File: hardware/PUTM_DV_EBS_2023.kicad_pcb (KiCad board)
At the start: 4 copper layers, 100 x 70 mm, 147 parts, among them IC1 UCC2946DG4, IC2 SN74LVC1G74DCTR, IC3 SN74LVC1G74DCTR, IC4 ACT4533AYH-T, J1 SAFETY_SUPPLY, J2 SWDIO_CONN, J3 SENSORS, J4 VALVES, J5 MAIN, K1 FINDER-30.22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

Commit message: wip
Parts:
- added REF**: TestPoint_Pad_D1.5mm, TestPoint:TestPoint_Pad_D1.5mm, F.Cu at (132.4, 107.8)
- C23: footprint Capacitor_SMD:C_0201_0603Metric_Pad0.64x0.40mm_HandSolder -> Capacitor_SMD:C_0603_1608Metric_Pad1.08x0.95mm_HandSolder
- moved G*** 113.5 mm to (120.7, 74.2), turned to 180 degrees
- moved REF** 85.6 mm to (136.5, 62.0), turned to 180 degrees
- moved C5 82.7 mm to (151.9, 42.7), turned to 90 degrees
- moved D15 63.6 mm to (157.7, 67.8)
- moved C31 63.6 mm to (154.9, 65.0)
- moved R32 63.6 mm to (158.0, 65.0)
- moved R33 63.6 mm to (156.5, 65.0)
- moved R30 58.2 mm to (141.7, 77.1), turned to -90 degrees
- moved R31 57.1 mm to (140.2, 77.1), turned to 90 degrees
- moved C30 56.0 mm to (138.7, 77.1), turned to 90 degrees
- moved R4 55.5 mm to (130.2, 73.6), turned to 0 degrees
- moved D14 55.4 mm to (140.4, 79.9), turned to 0 degrees
- moved R1 54.2 mm to (130.2, 75.4), turned to 0 degrees
- moved R14 52.8 mm to (130.2, 77.2), turned to 180 degrees
- moved R28 51.8 mm to (140.1, 82.7), turned to -90 degrees
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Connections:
- R47 pad 2: unconnected-(R47-Pad2) -> GND
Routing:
- net GND: track 74.9 -> 137.5 mm, vias 9 -> 17
- net Net-(IC1-Pad5): track 0.00 -> 37.6 mm
- net /EBS Logic/RESET BUTTON LATCH: track 0.00 -> 37.5 mm, vias 0 -> 3
- net /EBS Logic/AS COMMANDS OK: track 0.00 -> 30.4 mm, vias 0 -> 2
- net /EBS Supervisor/ERROR: track 0.00 -> 25.5 mm
- net /EBS Supervisor/CHECKUP: track 0.00 -> 24.7 mm, vias 0 -> 2
- net +3V3: track 2.21 -> 26.7 mm, vias 0 -> 2
- net VALVE_1_COIL_I: track 6.64 -> 26.3 mm
- net /EBS Logic/WATCHDOG: track 0.00 -> 18.3 mm, vias 0 -> 2
- net Net-(D12-Pad2): track 0.00 -> 17.7 mm
- net /EBS Supervisor/WARNING: track 0.00 -> 17.4 mm
- net /EBS Supervisor/OK: track 0.00 -> 15.4 mm, vias 0 -> 2
- net Net-(IC2-Pad3): track 0.00 -> 15.0 mm
- net Net-(IC3-Pad6): track 0.00 -> 14.5 mm
- net +24V: track 13.4 -> 25.4 mm
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
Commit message: fixed references addet tp;s mam pojutrze przejebany egzamin nara
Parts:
- removed the REF** at (132.4, 107.8)
- added C37: 100nF, Capacitor_SMD:C_0603_1608Metric, F.Cu at (109.7, 50.5)
- added C38: 100nF, Capacitor_SMD:C_0603_1608Metric, F.Cu at (103.6, 48.5)
- added C39: 100nF, Capacitor_SMD:C_0603_1608Metric, F.Cu at (103.4, 60.2)
- added NT1: NetTie_2, NetTie:NetTie-2_SMD_Pad0.5mm, F.Cu at (105.4, 72.9)
- added REF**: TestPoint_Pad_1.0x1.0mm, TestPoint:TestPoint_Pad_1.0x1.0mm, F.Cu at (187.2, 88.1)
- added REF**: TestPoint_Pad_1.0x1.0mm, TestPoint:TestPoint_Pad_1.0x1.0mm, F.Cu at (187.2, 81.3)
- added REF**: TestPoint_Pad_1.0x1.0mm, TestPoint:TestPoint_Pad_1.0x1.0mm, F.Cu at (187.2, 76.7)
- added REF**: TestPoint_Pad_1.0x1.0mm, TestPoint:TestPoint_Pad_1.0x1.0mm, F.Cu at (187.2, 83.6)
- added REF**: TestPoint_Pad_1.0x1.0mm, TestPoint:TestPoint_Pad_1.0x1.0mm, F.Cu at (181.9, 88.1)
- added REF**: TestPoint_Pad_1.0x1.0mm, TestPoint:TestPoint_Pad_1.0x1.0mm, F.Cu at (187.2, 85.9)
- added REF**: TestPoint_Pad_1.0x1.0mm, TestPoint:TestPoint_Pad_1.0x1.0mm, F.Cu at (181.9, 76.7)
- added REF**: TestPoint_Pad_1.0x1.0mm, TestPoint:TestPoint_Pad_1.0x1.0mm, F.Cu at (187.2, 79.0)
- added REF**: TestPoint_Pad_1.0x1.0mm, TestPoint:TestPoint_Pad_1.0x1.0mm, F.Cu at (181.9, 81.3)
- added REF**: TestPoint_Pad_1.0x1.0mm, TestPoint:TestPoint_Pad_1.0x1.0mm, F.Cu at (181.9, 83.6)
- added REF**: TestPoint_Pad_1.0x1.0mm, TestPoint:TestPoint_Pad_1.0x1.0mm, F.Cu at (181.9, 79.0)
- added REF**: TestPoint_Pad_1.0x1.0mm, TestPoint:TestPoint_Pad_1.0x1.0mm, F.Cu at (181.9, 85.9)
- C18: footprint Capacitor_SMD:C_0805_2012Metric_Pad1.18x1.45mm_HandSolder -> Capacitor_SMD:C_1206_3216Metric
- moved G*** 71.7 mm to (172.8, 94.2)
- moved D2 28.6 mm to (124.5, 37.8), turned to -135 degrees
- moved R13 20.8 mm to (125.2, 40.6), turned to 45 degrees
- moved JP1 12.4 mm to (119.4, 42.2), turned to 90 degrees
- moved R5 11.0 mm to (130.0, 73.7)
- moved R4 10.7 mm to (130.0, 84.3)
- moved C14 9.85 mm to (112.8, 59.4), turned to 180 degrees
- moved C15 9.68 mm to (106.3, 56.0)
- moved U6 9.67 mm to (110.7, 55.9)
- moved R46 6.93 mm to (96.8, 60.2), turned to 90 degrees
- moved R44 4.52 mm to (100.3, 54.6), turned to 180 degrees
- moved U10 3.65 mm to (100.1, 60.2), turned to 0 degrees
- moved C19 3.31 mm to (148.6, 57.7), turned to -90 degrees
- moved K2 3.25 mm to (165.1, 50.5)
- moved R43 3.07 mm to (97.0, 48.6)
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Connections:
- net /EBS Supervisor/CAN_RX+ renamed /EBS Supervisor/(CAN_RX)+
- net /EBS Supervisor/CAN_TX- renamed /EBS Supervisor/(CAN_TX)-
- J3 pad 1: AIR_MAIN -> AIR_EBS
- J3 pad 2: AIR_EBS -> AIR_MAIN
- R4 pad 2: /EBS Logic/WATCHDOG -> /EBS Logic/AS_CLOSE_SDC
- R5 pad 2: /EBS Logic/AS_CLOSE_SDC -> /EBS Logic/WATCHDOG
- REF** pad 1: (no net) -> GND
- U5 pad 10: /Air pressure sensor control/MAIN -> /Air pressure sensor control/REDUNDANT
- U5 pad 8: /Air pressure sensor control/REDUNDANT -> /Air pressure sensor control/MAIN
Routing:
- net /Air pressure sensor control/MAIN: track 0.00 -> 69.5 mm, vias 0 -> 2
- net /Air pressure sensor control/EBS: track 0.00 -> 50.8 mm
- net /Air pressure sensor control/REDUNDANT: track 0.00 -> 38.9 mm
- net +24V: track 25.4 -> 58.8 mm
- net /EBS Logic/RESET BUTTON LATCH: track 37.5 -> 6.04 mm, vias 3 -> 2
- net VALVE_2_COIL_I: track 6.15 -> 34.6 mm
- net Net-(IC1-Pad5): track 37.6 -> 17.8 mm
- net NRST: track 0.00 -> 16.7 mm
- net AUX1: track 0.00 -> 13.6 mm
- net CAN+: track 19.5 -> 6.48 mm
- net /EBS Logic/AS COMMANDS OK: track 30.4 -> 17.9 mm, vias 2 -> 0
- net Net-(U5-Pad21): track 0.00 -> 12.2 mm
- net CAN-: track 17.3 -> 5.92 mm, vias 2 -> 0
- net SWDCLK: track 0.00 -> 11.2 mm
- net AUX2: track 0.00 -> 11.0 mm
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- added copper zone on F.Cu, net +24V
- added copper zone on B.Cu, net +5V
- added copper zone on F.Cu, net +5V
- added copper zone on F.Cu, net /Power Supply/SW_loop
- added copper zone on F.Cu, net GND
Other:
- board text added: "AND2"
- board text added: "NAND1"
- board text added: "RST_EBS"
- board text added: "RST_LATCH"
- board text added: "RTH"
- board text added: "SDC_IN"
- board text added: "SDC_K"
- board text added: "SDC_RDY"
- board text added: "TSON_DRV"
- board text added: "TSON_EXT"
- board text added: "WDI"
- board text added: "WDO"

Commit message: supply section redesign due to IC shortage
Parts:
- removed C17: 47uF, Capacitor_SMD:CP_Elec_6.3x7.7
- removed C18: 10uF low ESR, Capacitor_SMD:C_1206_3216Metric
- removed C21: 2.2nF, Capacitor_SMD:C_0603_1608Metric_Pad1.08x0.95mm_HandSolder
- removed C22: 22nF, Capacitor_SMD:C_1206_3216Metric
- removed C24: 1nF, Capacitor_SMD:C_0603_1608Metric_Pad1.08x0.95mm_HandSolder
- removed C25: 10uF, Capacitor_SMD:C_0603_1608Metric_Pad1.08x0.95mm_HandSolder
- removed C26: 220uF, Capacitor_SMD:CP_Elec_6.3x7.7
- removed IC4: ACT4533AYH-T, SamacSys_Parts:SOIC127P600X170-9N
- removed L2: 47uH, PUTM_Kicad_FOOTPRINTS:L_Bourns_SRP1038WA
- removed R20, R21: 15k, Resistor_SMD:R_0603_1608Metric_Pad0.98x0.95mm_HandSolder
- removed R22: 100k, Resistor_SMD:R_0603_1608Metric_Pad0.98x0.95mm_HandSolder
- removed R23: 9,76k, Resistor_SMD:R_0603_1608Metric_Pad0.98x0.95mm_HandSolder
- removed R24: 51k, Resistor_SMD:R_0603_1608Metric_Pad0.98x0.95mm_HandSolder
- removed the REF** at (136.5, 62.0)
- added Cb_infltr1: 4,7uF 3Ohm, Capacitor_SMD:CP_Elec_4x5.4, F.Cu at (163.1, 139.1)
- added Cboot1: 100nF 1mOhm, Capacitor_SMD:C_0402_1005Metric_Pad0.74x0.62mm_HandSolder, F.Cu at (159.0, 150.6)
- added Cf_infltr: 10uF 1mOhm, Capacitor_SMD:C_1210_3225Metric_Pad1.33x2.70mm_HandSolder, F.Cu at (134.4, 46.0)
- added Cf_infltr1: 10uF 1mOhm, Capacitor_SMD:C_1210_3225Metric_Pad1.33x2.70mm_HandSolder, F.Cu at (138.9, 45.0)
- added Cf_infltr2: 10uF 1mOhm, Capacitor_SMD:C_1210_3225Metric_Pad1.33x2.70mm_HandSolder, F.Cu at (143.3, 46.0)
- added Cin1: 4,7uF 1mOhm, Capacitor_SMD:C_0805_2012Metric_Pad1.18x1.45mm_HandSolder, F.Cu at (169.4, 137.7)
- added Cinx1: 100nF 64mOhm, Capacitor_SMD:C_0805_2012Metric_Pad1.18x1.45mm_HandSolder, F.Cu at (176.2, 131.1)
- added Cout1: 47uF 3,037mOhm, Capacitor_SMD:C_1206_3216Metric_Pad1.33x1.80mm_HandSolder, F.Cu at (170.8, 131.3)
- added Cout1: 47uF 3,037mOhm, Capacitor_SMD:C_1206_3216Metric_Pad1.33x1.80mm_HandSolder, F.Cu at (173.2, 127.0)
- added F1: 1A, Fuse:Fuse_1206_3216Metric, F.Cu at (157.0, 148.0)
- added LF_infltr1: 1.5uH 260mOhm, Inductor_SMD:L_0805_2012Metric_Pad1.05x1.20mm_HandSolder, F.Cu at (197.1, 107.2)
- added L_SW1: 18uH 36mOhm, PUTM_Kicad_FOOTPRINTS:L_Bourns_EBS, F.Cu at (150.7, 136.2)
- added Rd_infltr1: 0.1R, Resistor_SMD:R_0603_1608Metric_Pad0.98x0.95mm_HandSolder, F.Cu at (161.9, 147.5)
- added Rfbb1: 10kOhm, Resistor_SMD:R_0402_1005Metric_Pad0.72x0.64mm_HandSolder, F.Cu at (180.2, 130.6)
- added Rfbt1: 23,2kOhm, Resistor_SMD:R_0402_1005Metric_Pad0.72x0.64mm_HandSolder, F.Cu at (155.8, 150.6)
- added Rpgood1: 100kOhm, Resistor_SMD:R_0603_1608Metric_Pad0.98x0.95mm_HandSolder, F.Cu at (174.0, 137.0)
- added Rt1: 64,9kOhm, Resistor_SMD:R_0603_1608Metric_Pad0.98x0.95mm_HandSolder, F.Cu at (169.2, 140.4)
- added U11: LMR38010SDDAR, Package_SO:TI_SO-PowerPAD-8_ThermalVias, F.Cu at (163.5, 132.9)
- D9: value SK54BL -> LED 5V; footprint Diode_SMD:D_SMB -> LED_SMD:LED_0603_1608Metric_Pad1.05x0.95mm_HandSolder
- R18: value 7,5k -> 1k
- moved D9 90.4 mm to (167.5, 143.3)
- moved R18 87.3 mm to (176.0, 133.9)
- moved G*** 51.6 mm to (100.6, 121.7)
- moved REF** 39.8 mm to (130.6, 94.1)
- moved D11 13.0 mm to (160.3, 92.8)
- moved D18 13.0 mm to (151.1, 92.8)
- moved D8 13.0 mm to (155.7, 92.8)
- moved R19 13.0 mm to (155.7, 96.4)
- moved R26 13.0 mm to (160.3, 96.4)
- moved R37 13.0 mm to (151.1, 96.4)
- moved D16 13.0 mm to (137.2, 92.8)
- moved R35 13.0 mm to (137.2, 96.4)
- moved D17 13.0 mm to (142.0, 92.8)
- moved D6 13.0 mm to (146.6, 92.8)
- moved R36 13.0 mm to (142.0, 96.4)
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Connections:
- D9 pad 1: /Power Supply/SW_loop -> Net-(D9-Pad1)
- D9 pad 2: GND -> +5V
- R18 pad 1: Net-(IC4-Pad8) -> GND
- R18 pad 2: GND -> Net-(D9-Pad1)
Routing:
- net +24V: track 58.8 -> 13.4 mm
- net AUX1: track 13.6 -> 56.8 mm, vias 0 -> 2
- net AUX2: track 11.0 -> 54.0 mm, vias 0 -> 2
- net GND: track 136.3 -> 112.8 mm, vias 22 -> 12
- net /Air pressure sensor control/MAIN: track 69.5 -> 47.8 mm
- net /EBS Supervisor/CHECKUP: track 24.7 -> 5.87 mm, vias 2 -> 0
- net /EBS Supervisor/ERROR: track 25.5 -> 6.94 mm
- net /Air pressure sensor control/EBS: track 50.8 -> 35.8 mm
- net /Air pressure sensor control/REDUNDANT: track 38.9 -> 24.3 mm
- net CAN-: track 5.92 -> 18.8 mm
- net CAN+: track 6.48 -> 18.6 mm
- net /EBS Logic/AS COMMANDS OK: track 17.9 -> 6.89 mm
- net /EBS Logic/WATCHDOG: track 15.0 -> 3.98 mm, vias 1 -> 0
- net EBS_RESET _BUTTON: track 0.00 -> 9.48 mm
- net /EBS Supervisor/WARNING: track 17.4 -> 8.51 mm
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- removed copper zone on F.Cu, net +24V
- removed copper zone on B.Cu, net +5V
- removed copper zone on F.Cu, net +5V
- removed copper zone on F.Cu, net /Power Supply/SW_loop
- removed copper zone on F.Cu, net GND
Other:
- rule pad_to_mask_clearance: 0.05 -> 0
- board text removed: "LED's"
- board text removed: "logic"

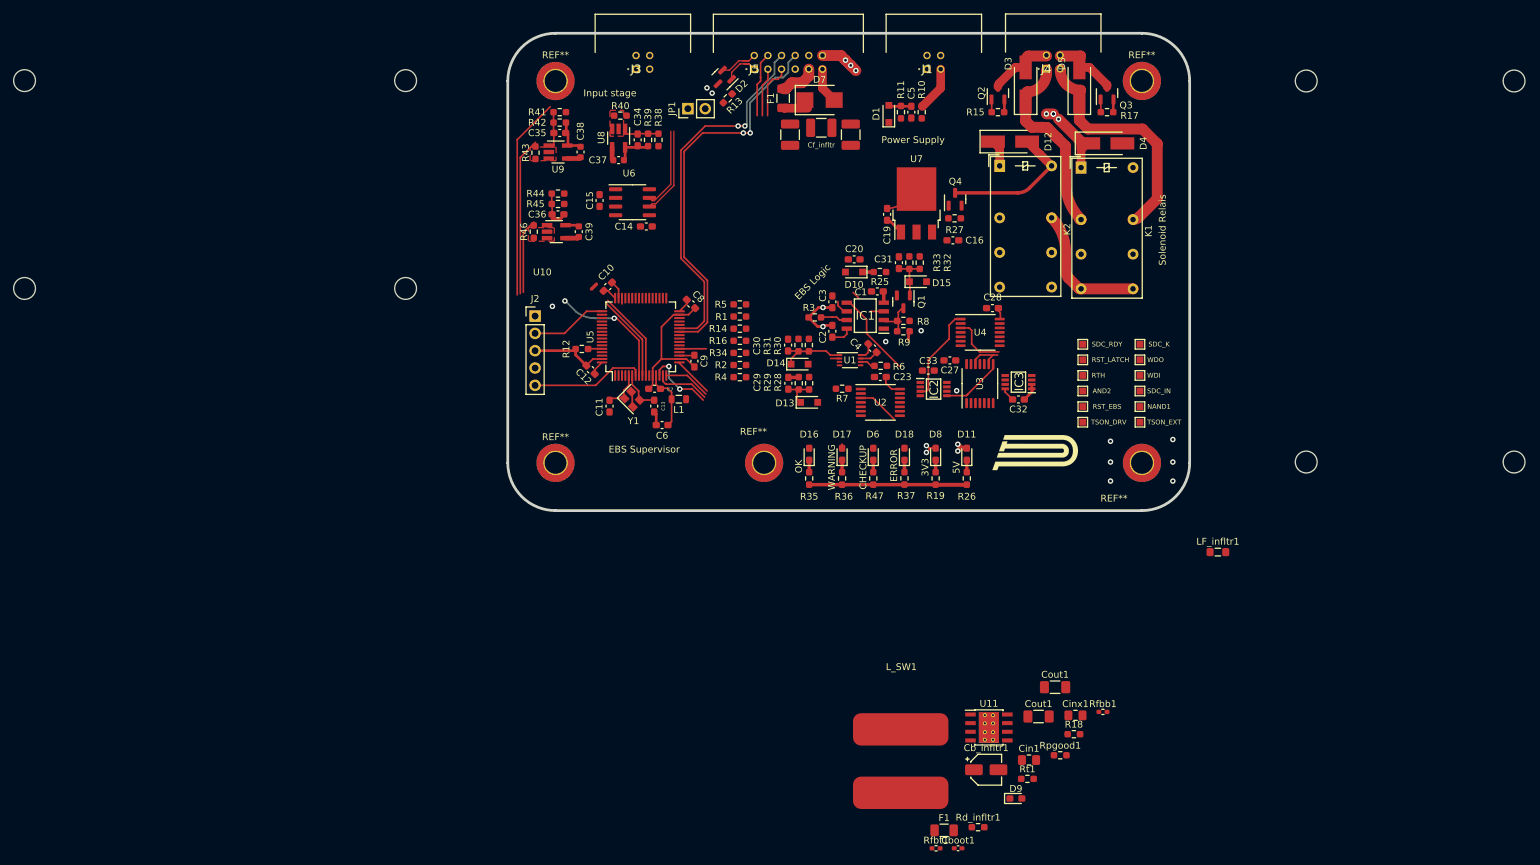
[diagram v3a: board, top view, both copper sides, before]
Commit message: routing update, new supply section routed
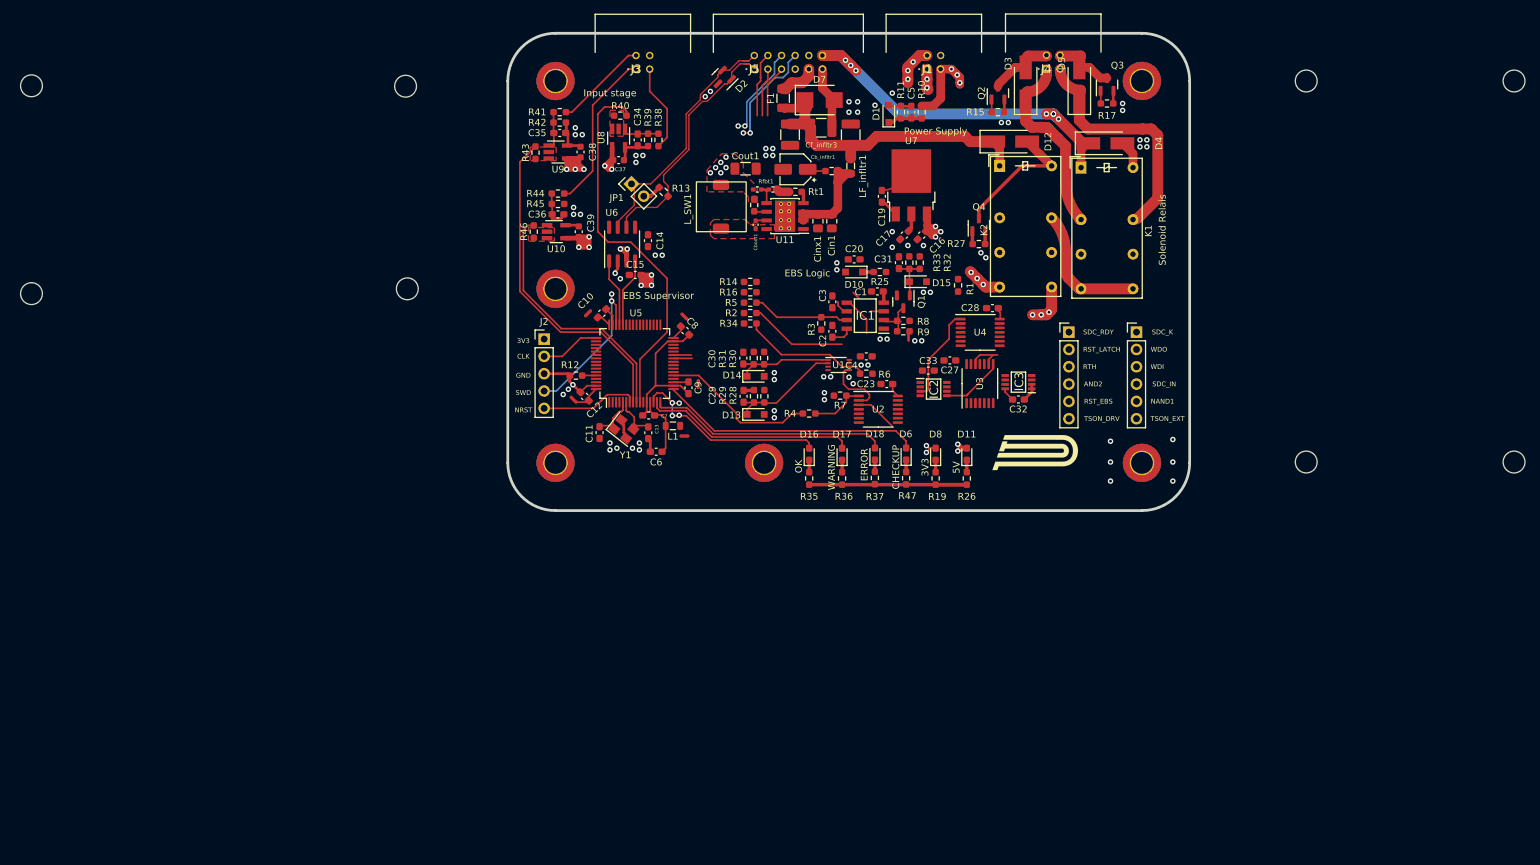
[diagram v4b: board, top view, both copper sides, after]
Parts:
- removed the Cout1 at (173.2, 127.0)
- removed D9: LED 5V, LED_SMD:LED_0603_1608Metric_Pad1.05x0.95mm_HandSolder
- removed the F1 at (157.0, 148.0)
- removed R18: 1k, Resistor_SMD:R_0603_1608Metric_Pad0.98x0.95mm_HandSolder
- removed the REF** at (185.7, 88.1)
- removed the REF** at (185.7, 81.3)
- removed the REF** at (185.7, 76.7)
- removed the REF** at (185.7, 83.6)
- removed the REF** at (177.3, 88.1)
- removed the REF** at (185.7, 85.9)
- removed the REF** at (177.3, 76.7)
- removed the REF** at (185.7, 79.0)
- removed the REF** at (177.3, 81.3)
- removed the REF** at (177.3, 83.6)
- removed the REF** at (177.3, 79.0)
- removed the REF** at (177.3, 85.9)
- added C17: 100n, Capacitor_SMD:C_0603_1608Metric_Pad1.08x0.95mm_HandSolder, F.Cu at (151.1, 60.7)
- added NT1: NetTie_2, NetTie:NetTie-2_SMD_Pad0.5mm, F.Cu at (118.9, 72.6)
- added NT1: NetTie_2, NetTie:NetTie-2_SMD_Pad0.5mm, F.Cu at (118.9, 90.2)
- added NT1: NetTie_2, NetTie:NetTie-2_SMD_Pad0.5mm, F.Cu at (120.9, 82.5)
- added NT1: NetTie_2, NetTie:NetTie-2_SMD_Pad0.5mm, F.Cu at (102.6, 84.8)
- added REF**: PinHeader_1x06_P2.54mm_Vertical, Connector_PinHeader_2.54mm:PinHeader_1x06_P2.54mm_Vertical, F.Cu at (185.2, 74.9)
- added REF**: MountingHole_3.2mm_M3_DIN965_Pad_TopBottom, MountingHole:MountingHole_3.2mm_M3_DIN965_Pad_TopBottom, F.Cu at (100.0, 68.6)
- added REF**: PinHeader_1x06_P2.54mm_Vertical, Connector_PinHeader_2.54mm:PinHeader_1x06_P2.54mm_Vertical, F.Cu at (175.3, 74.9)
- L_SW1: value 18uH 36mOhm -> 22uH 36mOhm
- Y1: footprint Crystal:Crystal_SMD_2520-4Pin_2.5x2.0mm -> Crystal:Crystal_SMD_3225-4Pin_3.2x2.5mm
- moved Rfbt1 100.1 mm to (129.6, 54.0)
- moved Rd_infltr1 98.6 mm to (140.5, 51.3), turned to 180 degrees
- moved Cboot1 96.1 mm to (129.3, 59.2), turned to -90 degrees
- moved Rt1 92.6 mm to (135.2, 54.4), turned to 180 degrees
- moved Cb_infltr1 92.4 mm to (135.2, 51.1), turned to 180 degrees
- moved Rpgood1 92.3 mm to (129.1, 56.3), turned to 90 degrees
- moved Cout1 91.1 mm to (127.8, 51.0)
- moved Rfbb1 90.6 mm to (131.8, 54.0)
- moved Cin1 84.1 mm to (140.5, 58.7), turned to -90 degrees
- moved L_SW1 83.3 mm to (124.2, 57.1), turned to 90 degrees
- moved Cinx1 81.7 mm to (138.5, 58.7), turned to -90 degrees
- moved U11 80.7 mm to (133.6, 57.9), turned to 180 degrees
- moved LF_infltr1 78.2 mm to (143.3, 50.5), turned to -90 degrees
- moved R1 32.3 mm to (159.0, 68.1), turned to -90 degrees
- moved R13 16.6 mm to (115.8, 54.4), turned to -45 degrees
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- renumbered Cf_infltr to Cf_infltr3
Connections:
- net Net-(Cboot1-Pad1) renamed /Power Supply/BOOT
- net Net-(Cboot1-Pad2) renamed /Power Supply/SW
- net Net-(Rfbb1-Pad1) renamed /Power Supply/FB_point
- net Net-(Rpgood1-Pad1) renamed /Power Supply/Pgoood
- net Net-(Rt1-Pad1) renamed /Power Supply/Rt
- J3 pad 1: AIR_EBS -> AIR_REDUNDANT
- J3 pad 3: AIR_REDUNDANT -> AIR_EBS
- U5 pad 10: /Air pressure sensor control/REDUNDANT -> /Air pressure sensor control/MAIN
- U5 pad 8: /Air pressure sensor control/MAIN -> /Air pressure sensor control/EBS
- U5 pad 9: /Air pressure sensor control/EBS -> /Air pressure sensor control/REDUNDANT
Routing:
- net +5V: track 8.31 -> 175.9 mm, vias 2 -> 24
- net LINE: track 0.00 -> 60.9 mm, vias 0 -> 5
- net SAFETY_IN: track 6.59 -> 54.8 mm, vias 0 -> 6
- net +24V: track 13.4 -> 52.6 mm
- net SAFETY_OUT: track 0.00 -> 38.6 mm, vias 0 -> 3
- net AUX1: track 56.8 -> 18.6 mm
- net AUX2: track 54.0 -> 16.2 mm
- net /EBS Supervisor/CHECKUP: track 5.87 -> 38.4 mm
- net /EBS Supervisor/ERROR: track 6.94 -> 35.2 mm
- net AIR_REDUNDANT: track 0.00 -> 23.7 mm
- net /EBS Supervisor/WARNING: track 8.51 -> 31.6 mm
- net SWDIO: track 0.86 -> 23.7 mm, vias 1 -> 2
- net /EBS Supervisor/OK: track 10.5 -> 30.9 mm, vias 2 -> 4
- net CAN+: track 18.6 -> 38.1 mm
- net Net-(R4-Pad1): track 3.95 -> 22.9 mm
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- added copper zone on F.Cu, net +5V
- added copper zone on F.Cu, net /Power Supply/SW
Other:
- board text added: "CLK"
- board text added: "GND"
- board text added: "NRST"
- board text added: "SWD"
- board text added: "if doesn't work +48 739 064 384 hrs: 9PM-3AM (connection fee in accordance with the operator's tariff)"
- board text removed: "if doesn't work +48 739 064 384 (connection fee in accordance with the operator's tariff)"
